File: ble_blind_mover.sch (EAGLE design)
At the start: 47 parts, among them J1 105017-0001, Q1 DMG6968U-7, Q2 DMG6968U-7, U1 MIC5205-3.3YM5-TR, U2 YJ-14015, U3 VIPER012LS

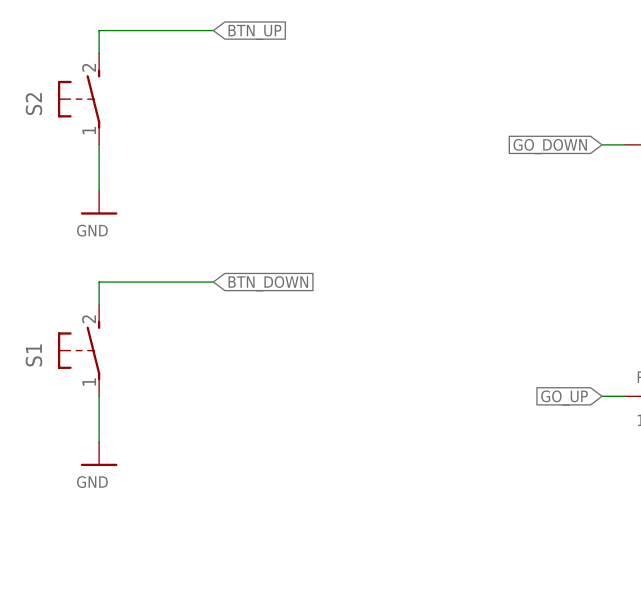
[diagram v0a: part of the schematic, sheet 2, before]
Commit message: Naming all nets
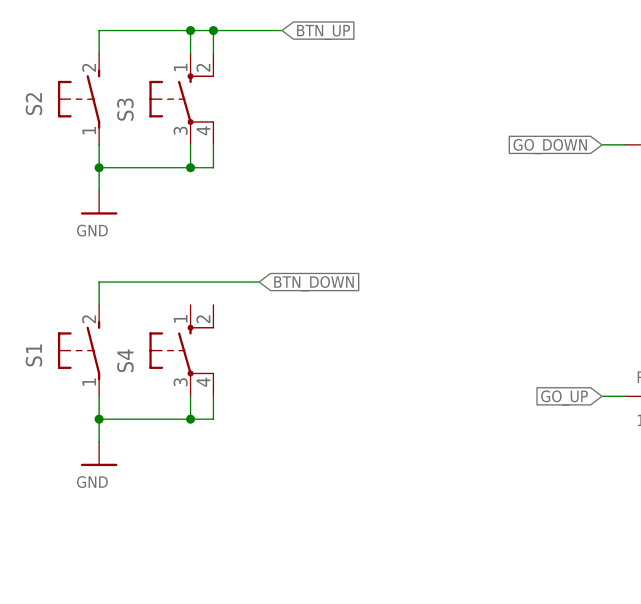
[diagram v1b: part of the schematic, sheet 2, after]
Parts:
- added S3, S4: (no value), switch-omron:10-XX
- CON_AC_IN: device con-ptr500:AK300/2 -> con-ptr500:AK500/2
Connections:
- net N$1 renamed VIPER_OUT
- net N$2 renamed VIPER_VCC
- net N$3 renamed VIPER_PRE_FB
- net N$4 renamed VIPER_FB
- net N$5 renamed LINE_RECTIFIED
- net N$6 renamed LINE_FILTERED
- net N$7 renamed VIPER_COMP
- net N$8 renamed VIPER_COMP_MID
- net N$9 renamed LINE_RECTIFIED_R
- removed net N$10: RELAY2.11
- net BTN_UP: now also S3.S, S3.S1
- net GND: now also S3.P, S3.P1, S4.P, S4.P1
- net NEUTRAL: now also RELAY2.11
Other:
- moved on the sheet: D1
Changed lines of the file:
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@@
 <part name="GND5" library="logic-supply" deviceset="GND" device=""/>
 <part name="SWD" library="con-molex" deviceset="53?-04" device="047"/>
-<part name="CON_AC_IN" library="con-ptr500" deviceset="AK300/2" device=""/>
+<part name="CON_AC_IN" library="con-ptr500" deviceset="AK500/2" device=""/>
 <part name="CON_BLIND" library="con-ptr500" deviceset="AK500/3" device=""/>
 <part name="U3" library="st_viper" deviceset="VIPER012LS" device=""/>
@@
 <part name="GND13" library="supply1" deviceset="GND" device=""/>
 <part name="GND19" library="supply1" deviceset="GND" device=""/>
+<part name="S3" library="switch-omron" deviceset="10-XX" device=""/>
+<part name="S4" library="switch-omron" deviceset="10-XX" device=""/>
 </parts>
 <sheets>
@@
 <attribute name="VALUE" x="69.85" y="146.939" size="1.27" layer="96" font="vector"/>
 </instance>
-<instance part="D1" gate="G$1" x="88.9" y="149.86" smashed="yes">
-<attribute name="NAME" x="86.614" y="151.3586" size="1.6764" layer="95" ratio="12"/>
-<attribute name="VALUE" x="86.868" y="146.7866" size="1.6764" layer="96"/>
+<instance part="D1" gate="G$1" x="91.44" y="149.86" smashed="yes">
+<attribute name="NAME" x="89.154" y="151.3586" size="1.6764" layer="95" ratio="12"/>
+<attribute name="VALUE" x="89.408" y="146.7866" size="1.6764" layer="96"/>
 </instance>
 <instance part="R1" gate="G$1" x="104.14" y="149.86" smashed="yes">
@@
 <wire x1="132.08" y1="139.7" x2="132.08" y2="137.16" width="0.1524" layer="91"/>
 <junction x="132.08" y="137.16"/>
-<wire x1="70.9676" y1="91.44" x2="91.44" y2="91.44" width="0.1524" layer="91"/>
 <wire x1="91.44" y1="91.44" x2="91.44" y2="137.16" width="0.1524" layer="91"/>
 <junction x="91.44" y="137.16"/>
@@
 <wire x1="68.58" y1="45.72" x2="91.44" y2="45.72" width="0.1524" layer="91"/>
 <wire x1="91.44" y1="45.72" x2="91.44" y2="91.44" width="0.1524" layer="91"/>
+<pinref part="RELAY2" gate="G$1" pin="11"/>
+<wire x1="68.58" y1="91.44" x2="91.44" y2="91.44" width="0.1524" layer="91"/>
 <junction x="91.44" y="91.44"/>
 </segment>
@@
 <segment>
 <pinref part="D1" gate="G$1" pin="A"/>
-<wire x1="86.36" y1="149.86" x2="78.74" y2="149.86" width="0.1524" layer="91"/>
+<wire x1="88.9" y1="149.86" x2="83.82" y2="149.86" width="0.1524" layer="91"/>
 <pinref part="FUSE_MAINS" gate="1" pin="2"/>
-</segment>
-</net>
-<net name="N$5" class="0">
+<wire x1="83.82" y1="149.86" x2="78.74" y2="149.86" width="0.1524" layer="91"/>
+<wire x1="83.82" y1="149.86" x2="88.9" y2="149.86" width="0.1524" layer="91"/>
+<junction x="83.82" y="149.86"/>
+<wire x1="83.82" y1="157.48" x2="91.44" y2="157.48" width="0.1524" layer="91"/>
+<wire x1="83.82" y1="149.86" x2="83.82" y2="157.48" width="0.1524" layer="91"/>
+<label x="91.44" y="157.48" size="1.27" layer="95" font="vector" xref="yes"/>
+</segment>
+</net>
+<net name="LINE_RECTIFIED" class="0">
 <segment>
 <pinref part="R1" gate="G$1" pin="1"/>
 <pinref part="D1" gate="G$1" pin="C"/>
-<wire x1="99.06" y1="149.86" x2="91.44" y2="149.86" width="0.1524" layer="91"/>
-</segment>
-</net>
-<net name="N$2" class="0">
+<wire x1="99.06" y1="149.86" x2="93.98" y2="149.86" width="0.1524" layer="91"/>
+</segment>
+</net>
+<net name="VIPER_VCC" class="0">
 <segment>
 <pinref part="U3" gate="G$1" pin="VCC"/>
@@
 </segment>
 </net>
-<net name="N$1" class="0">
+<net name="VIPER_OUT" class="0">
 <segment>
 <pinref part="D3" gate="G$1" pin="C"/>
@@
 </segment>
 </net>
-<net name="N$3" class="0">
+<net name="VIPER_PRE_FB" class="0">
 <segment>
 <pinref part="R11" gate="G$1" pin="2"/>
@@
 </segment>
 </net>
-<net name="N$4" class="0">
+<net name="VIPER_FB" class="0">
 <segment>
 <pinref part="R11" gate="G$1" pin="1"/>
@@
 </segment>
 </net>
-<net name="N$7" class="0">
+<net name="VIPER_COMP" class="0">
 <segment>
 <pinref part="R14" gate="G$1" pin="2"/>
@@
 </segment>
 </net>
-<net name="N$8" class="0">
+<net name="VIPER_COMP_MID" class="0">
 <segment>
 <pinref part="C6" gate="G$1" pin="1"/>
@@
 </segment>
 </net>
-<net name="N$6" class="0">
+<net name="LINE_FILTERED" class="0">
 <segment>
 <pinref part="U3" gate="G$1" pin="DRAIN"/>
@@
 </segment>
 </net>
-<net name="N$9" class="0">
+<net name="LINE_RECTIFIED_R" class="0">
 <segment>
 <pinref part="L2" gate="G$1" pin="1"/>
@@
 <wire x1="111.76" y1="147.32" x2="111.76" y2="149.86" width="0.1524" layer="91"/>
 <junction x="111.76" y="149.86"/>
-</segment>
-</net>
-<net name="N$10" class="0">
-<segment>
-<pinref part="RELAY2" gate="G$1" pin="11"/>
-<wire x1="71.12" y1="91.44" x2="68.58" y2="91.44" width="0.1524" layer="91"/>
 </segment>
 </net>
@@
 <attribute name="VALUE" x="118.11" y="156.718" size="1.27" layer="96" font="vector" ratio="10"/>
 </instance>
+<instance part="S3" gate="1" x="30.48" y="157.48" smashed="yes">
+<attribute name="NAME" x="24.13" y="154.94" size="1.778" layer="95" rot="R90"/>
+<attribute name="VALUE" x="26.67" y="160.655" size="1.778" layer="96" rot="R90"/>
+</instance>
+<instance part="S4" gate="1" x="30.48" y="129.54" smashed="yes">
+<attribute name="NAME" x="24.13" y="127" size="1.778" layer="95" rot="R90"/>
+<attribute name="VALUE" x="26.67" y="132.715" size="1.778" layer="96" rot="R90"/>
+</instance>
 </instances>
 <busses>
@@
 <pinref part="GND4" gate="1" pin="GND"/>
 <pinref part="S1" gate="1" pin="P"/>
-<wire x1="20.32" y1="119.38" x2="20.32" y2="124.46" width="0.1524" layer="91"/>
+<wire x1="20.32" y1="119.38" x2="20.32" y2="121.92" width="0.1524" layer="91"/>
+<pinref part="S4" gate="1" pin="P"/>
+<wire x1="20.32" y1="121.92" x2="20.32" y2="124.46" width="0.1524" layer="91"/>
+<wire x1="30.48" y1="124.46" x2="30.48" y2="121.92" width="0.1524" layer="91"/>
+<wire x1="30.48" y1="121.92" x2="20.32" y2="121.92" width="0.1524" layer="91"/>
+<junction x="20.32" y="121.92"/>
+<wire x1="30.48" y1="121.92" x2="33.02" y2="121.92" width="0.1524" layer="91"/>
+<junction x="30.48" y="121.92"/>
+<pinref part="S4" gate="1" pin="P1"/>
+<wire x1="33.02" y1="121.92" x2="33.02" y2="124.46" width="0.1524" layer="91"/>
 </segment>
 <segment>
 <pinref part="GND8" gate="1" pin="GND"/>
 <pinref part="S2" gate="1" pin="P"/>
-<wire x1="20.32" y1="147.32" x2="20.32" y2="152.4" width="0.1524" layer="91"/>
+<wire x1="20.32" y1="147.32" x2="20.32" y2="149.86" width="0.1524" layer="91"/>
+<pinref part="S3" gate="1" pin="P"/>
+<wire x1="20.32" y1="149.86" x2="20.32" y2="152.4" width="0.1524" layer="91"/>
+<wire x1="30.48" y1="152.4" x2="30.48" y2="149.86" width="0.1524" layer="91"/>
+<wire x1="20.32" y1="149.86" x2="30.48" y2="149.86" width="0.1524" layer="91"/>
+<junction x="20.32" y="149.86"/>
+<wire x1="30.48" y1="149.86" x2="33.02" y2="149.86" width="0.1524" layer="91"/>
+<junction x="30.48" y="149.86"/>
+<pinref part="S3" gate="1" pin="P1"/>
+<wire x1="33.02" y1="149.86" x2="33.02" y2="152.4" width="0.1524" layer="91"/>
 </segment>
 <segment>
@@
 <pinref part="S1" gate="1" pin="S"/>
 <wire x1="20.32" y1="134.62" x2="20.32" y2="137.16" width="0.1524" layer="91"/>
-<wire x1="20.32" y1="137.16" x2="33.02" y2="137.16" width="0.1524" layer="91"/>
-<label x="33.02" y="137.16" size="1.27" layer="95" font="vector" xref="yes"/>
+<wire x1="20.32" y1="137.16" x2="38.1" y2="137.16" width="0.1524" layer="91"/>
+<label x="38.1" y="137.16" size="1.27" layer="95" font="vector" xref="yes"/>
 </segment>
 <segment>
@@
 <pinref part="S2" gate="1" pin="S"/>
 <wire x1="20.32" y1="162.56" x2="20.32" y2="165.1" width="0.1524" layer="91"/>
-<wire x1="20.32" y1="165.1" x2="33.02" y2="165.1" width="0.1524" layer="91"/>
-<label x="33.02" y="165.1" size="1.27" layer="95" font="vector" xref="yes"/>
-</segment>
-<segment>
+<wire x1="20.32" y1="165.1" x2="30.48" y2="165.1" width="0.1524" layer="91"/>
+<label x="40.64" y="165.1" size="1.27" layer="95" font="vector" xref="yes"/>
+<pinref part="S3" gate="1" pin="S"/>
+<wire x1="30.48" y1="165.1" x2="33.02" y2="165.1" width="0.1524" layer="91"/>
+<wire x1="33.02" y1="165.1" x2="40.64" y2="165.1" width="0.1524" layer="91"/>
+<wire x1="30.48" y1="162.56" x2="30.48" y2="165.1" width="0.1524" layer="91"/>
+<junction x="30.48" y="165.1"/>
+<pinref part="S3" gate="1" pin="S1"/>
+<wire x1="33.02" y1="162.56" x2="33.02" y2="165.1" width="0.1524" layer="91"/>
+<junction x="33.02" y="165.1"/>
+</segment>
+<segment>

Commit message: Daily save
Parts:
- added C13: 100nF, rcl:C-EUC0603
- added C14: TBD, rcl:C-EUC0603
- added D5: (no value), diode_:SCHOTTKY-DIODESOD123
- C15: VOLTAGE (none) -> 16V
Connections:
- removed net AGND: C15.-, R9.1
- removed net VIPER_OUT: D3.C, L1.1, U3.DIS, U3.GND
- new net VIPER_GND: C13.2, C7.2, D3.C, L1.1, U3.DIS, U3.GND
- net GND: no longer C4.2, C5.2, C6.2, C7.2, R13.1
- net NEUTRAL: now also C14.2, C15.-, C4.2, C5.2, C6.2, R13.1, R9.1
- net VIPER_FB: now also C14.1
- net VIPER_PRE_FB: now also D5.A
- net VIPER_VCC: now also C13.1, D5.C
- net VUSB: now also J1.VUSB; no longer J1.VDD
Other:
- note added: "+3V3 LDO"
- note added: "2 Relays"
- note added: "230V - 3V3 AC/DC converter"
- note added: "230V AC"
- note added: "3V3"
- note added: "Bleeding resistor"
- note added: "Blind moving tube motor"
- note added: "External biasing diode"
- note added: "Fuse"
- note added: "PI filter, 1/2 bridge rectifier"
- note added: "Phase + 2 switched neutral"
- note added: "VccOnMax 8.5V"
- note added: "nRF51822 module"
- note added: "uUSB socket"
- note added: "up/down"

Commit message: Brd routed, clearance adjustment still WIP
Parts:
- removed C12: 470pF, rcl:C-EUC0603
- removed C15: 100uF, resistor:CPOL-EUCT7343
- removed S1, S2: (no value), switch-omron:31-XX
- removed U1: MIC5205-3.3YM5-TR, LTC_By_element14_Batch_1:LT1761ES5-3.3TRMPBF
- added C16, C17: 1uF, rcl:C-EUC0603
- added C18: 470pF, rcl:C-EUC0603
- added D6: STTH1L06A, xCommonLib:SCHOTTKY_DIODESMA
- added J2: (no value), tag-connect:TC2030_SWD-MCP-NL
- added R15: 0, rcl:R-EU_0207/7
- added U4: MIC5205-3.3YM5-TR, LTC_By_element14_Batch_1:LT1761ES5-3.3TRMPBF
- C11: value 1uF -> 100uF; device rcl:C-EUC0603 -> rcl:C-EUC1812; NI_PN (none) -> 715929-01
- R9: device rcl:R-EU_R0603 -> rcl:R-EU_R1206
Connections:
- removed net N$11: C12.1, U1.BYP
- removed net VIPER_GND: C13.2, C7.2, D3.C, L1.1, U3.DIS, U3.GND
- new net +5V: C10.1, C11.1, C16.1, D4.A, D6.C, L1.2, R9.2, U4.!SHDN, U4.IN
- new net HOT_GND: C13.2, C14.2, C4.2, C5.2, C6.2, C7.2, D3.C, L1.1, R13.1, R15.2, U3.DIS, U3.GND
- new net N$1: C18.1, U4.BYP
- net +3V3: now also C17.1, J2.VCC, U4.OUT; no longer C11.1, C15.+, D4.A, L1.2, R9.2, U1.OUT
- net BTN_DOWN: now also S4.S, S4.S1; no longer S1.S
- net BTN_UP: no longer S2.S
- net GND: now also C16.2, C17.2, C18.2, J2.GND, R15.1, U4.GND; no longer C11.2, C12.2, S1.P, S2.P, U1.GND
- net LED_B: now also U2.P0.18; no longer U2.P0.19
- net LED_G: now also U2.P0.19; no longer U2.P0.18
- net NEUTRAL: now also C11.2; no longer C14.2, C15.-, C4.2, C5.2, C6.2, R13.1
- net SWDCLK: now also J2.SWCLK/TCK
- net SWDIO: now also J2.SWDIO/TMS
- net VUSB: now also D6.A; no longer C10.1, U1.IN, U1.~SHDN
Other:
- note added: "SWD connector"
- moved on the sheet: D4, U2

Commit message: Fixed board eouting for increased low/high voltage clearance
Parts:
- removed R15: 0, rcl:R-EU_0207/7
- added R16: 0, rcl:R-EU_0207/7
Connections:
- removed net HOT_GND: C13.2, C14.2, C4.2, C5.2, C6.2, C7.2, D3.C, L1.1, R13.1, R15.2, U3.DIS, U3.GND
- new net NEUTRAL_DISCONNECTABLE: C11.2, D3.A, R16.2, R9.1
- net GND: now also C13.2, C14.2, C4.2, C5.2, C6.2, C7.2, D3.C, L1.1, R13.1, U3.DIS, U3.GND; no longer R15.1
- net NEUTRAL: now also R16.1; no longer C11.2, D3.A, R9.1

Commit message: Added power connecting pinheads
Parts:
- added JP1, JP2: (no value), pinhead:PINHD-1X2
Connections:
- net NEUTRAL_DISCONNECTABLE renamed NEUTRAL_SEP
- net +3V3: now also JP1.1
- net +5V: now also JP2.1
- net GND: now also JP1.2, JP2.2
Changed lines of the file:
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@@
 <?xml version="1.0" encoding="utf-8"?>
 <!DOCTYPE eagle SYSTEM "eagle.dtd">
-<eagle version="9.3.2">
+<eagle version="9.5.2">
 <drawing>
 <settings>
@@
 <part name="GND1" library="supply1" deviceset="GND" device=""/>
 <part name="GND2" library="supply1" deviceset="GND" device=""/>
+<part name="JP1" library="pinhead" deviceset="PINHD-1X2" device=""/>
+<part name="GND12" library="supply1" deviceset="GND" device=""/>
+<part name="+3V9" library="supply1" deviceset="+3V3" device=""/>
+<part name="JP2" library="pinhead" deviceset="PINHD-1X2" device=""/>
+<part name="GND17" library="supply1" deviceset="GND" device=""/>
+<part name="P+4" library="supply1" deviceset="+5V" device=""/>
 </parts>
 <sheets>
@@
 </segment>
 </net>
-<net name="NEUTRAL_DISCONNECTABLE" class="4">
+<net name="NEUTRAL_SEP" class="4">
 <segment>
 <pinref part="R16" gate="G$1" pin="2"/>
@@
 <attribute name="VALUE" x="45.72" y="10.16" size="1.27" layer="96" font="vector" ratio="10" rot="MR0"/>
 </instance>
+<instance part="JP1" gate="G$1" x="121.92" y="35.56" smashed="yes">
+<attribute name="NAME" x="115.57" y="41.275" size="1.778" layer="95"/>
+<attribute name="VALUE" x="115.57" y="30.48" size="1.778" layer="96"/>
+</instance>
+<instance part="GND12" gate="1" x="114.3" y="30.48" smashed="yes">
+<attribute name="VALUE" x="111.76" y="27.94" size="1.778" layer="96"/>
+</instance>
+<instance part="+3V9" gate="G$1" x="114.3" y="43.18" smashed="yes">
+<attribute name="VALUE" x="111.76" y="45.72" size="1.778" layer="96"/>
+</instance>
+<instance part="JP2" gate="G$1" x="137.16" y="35.56" smashed="yes">
+<attribute name="NAME" x="130.81" y="41.275" size="1.778" layer="95"/>
+<attribute name="VALUE" x="130.81" y="30.48" size="1.778" layer="96"/>
+</instance>
+<instance part="GND17" gate="1" x="129.54" y="30.48" smashed="yes">
+<attribute name="VALUE" x="127" y="27.94" size="1.778" layer="96"/>
+</instance>
+<instance part="P+4" gate="1" x="129.54" y="43.18" smashed="yes">
+<attribute name="VALUE" x="129.54" y="44.45" size="1.778" layer="96" align="bottom-center"/>
+</instance>
 </instances>
 <busses>
@@
 <wire x1="43.18" y1="17.78" x2="43.18" y2="15.24" width="0.1524" layer="91"/>
 </segment>
+<segment>
+<pinref part="JP1" gate="G$1" pin="2"/>
+<wire x1="119.38" y1="35.56" x2="114.3" y2="35.56" width="0.1524" layer="91"/>
+<pinref part="GND12" gate="1" pin="GND"/>
+<wire x1="114.3" y1="35.56" x2="114.3" y2="33.02" width="0.1524" layer="91"/>
+</segment>
+<segment>
+<pinref part="JP2" gate="G$1" pin="2"/>
+<wire x1="134.62" y1="35.56" x2="129.54" y2="35.56" width="0.1524" layer="91"/>
+<pinref part="GND17" gate="1" pin="GND"/>
+<wire x1="129.54" y1="35.56" x2="129.54" y2="33.02" width="0.1524" layer="91"/>
+</segment>
 </net>
 <net name="SWDCLK" class="4">
@@
 <wire x1="43.18" y1="30.48" x2="43.18" y2="33.02" width="0.1524" layer="91"/>
 </segment>
+<segment>
+<pinref part="JP1" gate="G$1" pin="1"/>
+<wire x1="119.38" y1="38.1" x2="114.3" y2="38.1" width="0.1524" layer="91"/>
+<pinref part="+3V9" gate="G$1" pin="+3V3"/>
+<wire x1="114.3" y1="38.1" x2="114.3" y2="40.64" width="0.1524" layer="91"/>
+</segment>
 </net>
 <net name="GO_DOWN" class="4">
@@
 <pinref part="P+3" gate="1" pin="+5V"/>
 </segment>
-</net>
+<segment>
+<pinref part="JP2" gate="G$1" pin="1"/>
+<wire x1="134.62" y1="38.1" x2="129.54" y2="38.1" width="0.1524" layer="91"/>
+<wire x1="129.54" y1="38.1" x2="129.54" y2="40.64" width="0.1524" layer="91"/>
+<pinref part="P+4" gate="1" pin="+5V"/>
+</segment>
+</net>
